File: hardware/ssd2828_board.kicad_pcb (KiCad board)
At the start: 4 copper layers, 91.3 x 53.5 mm, 144 parts, among them IC1 TLV62568DBVR, IC2 MIC5501-3.0YM5-TR, IC3 TPS65131TRGERQ1, J1 FH35C-25S-0.3SHW_50_, J2 FH35C-25S-0.3SHW_50_, J3 Conn_01x34, J4 245863050104829+, J5 503548-1220, J6 FH35C-25S-0.3SHW_50_, J7 FH35C-25S-0.3SHW_50_, J8 FH35C-25S-0.3SHW_50_, U1 SSD2828QN4, U2 PAM2306DYPAA, U3 MIC3289, U4 LP3320, Y1 24mhz

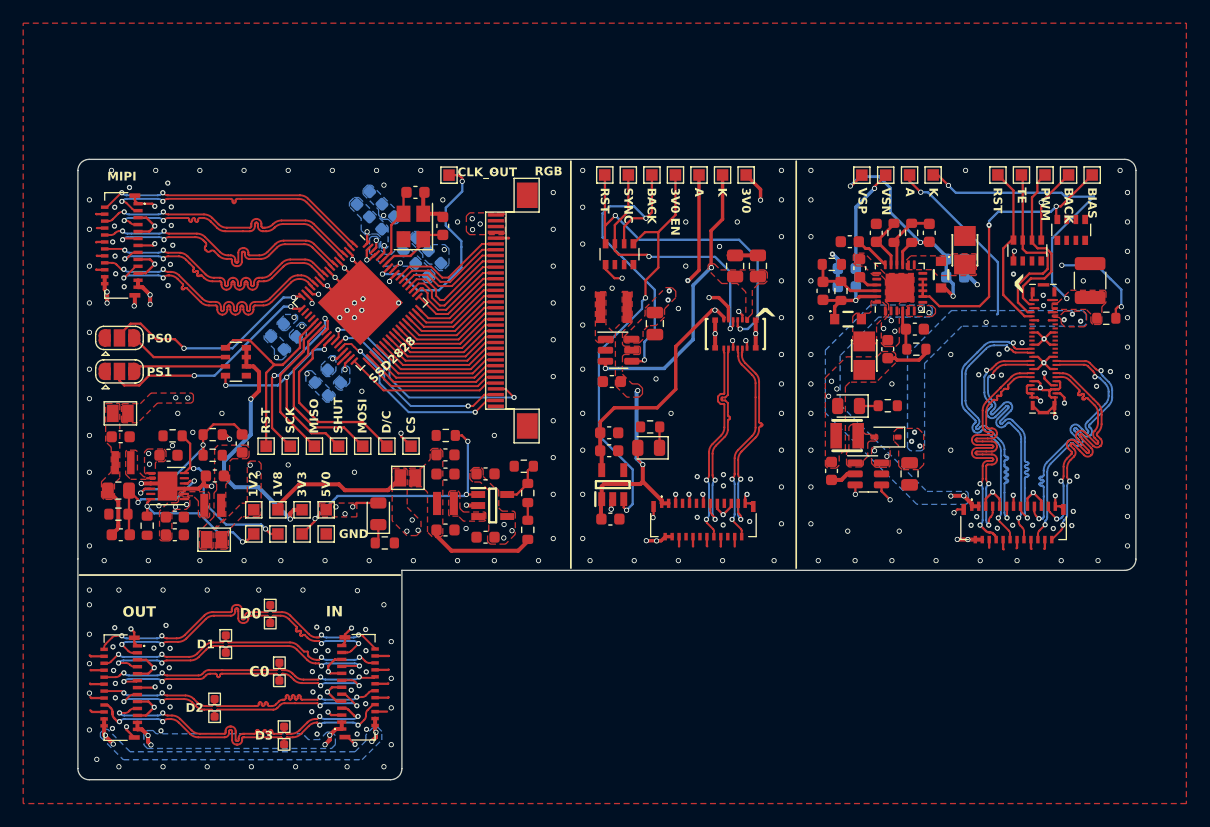
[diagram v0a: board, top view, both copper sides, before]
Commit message: added copper pour on back layer to adhere with jlcpcb guidelines
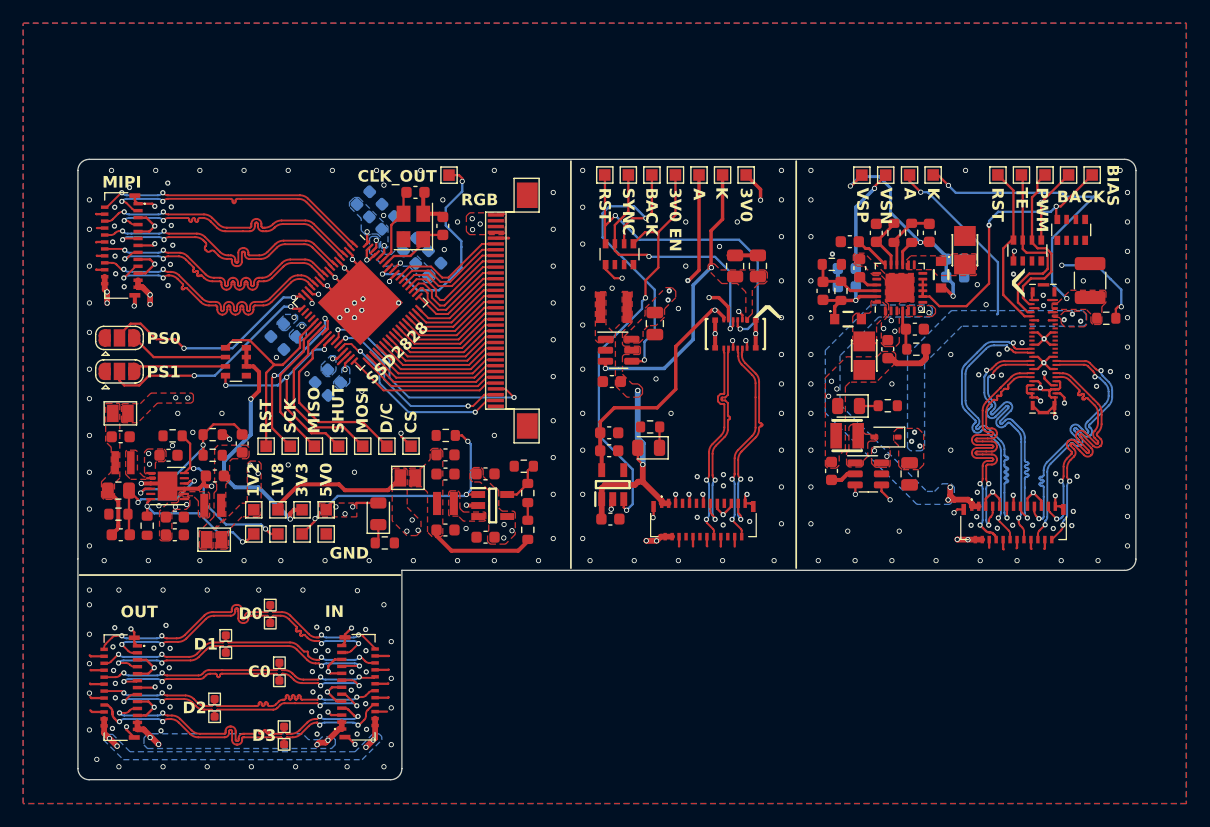
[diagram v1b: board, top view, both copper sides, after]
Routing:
- net GND: track 152.8 -> 148.4 mm
- net +5V: track 37.4 -> 39.9 mm
- net +1V8: track 81.4 -> 83.0 mm
- net /VS035ZSM/BIAS_EN: track 26.5 -> 25.8 mm

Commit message: fixed hirose FPC connector poinitng backwards on the 2 lcd boards+added stm32f401 boilerplate code
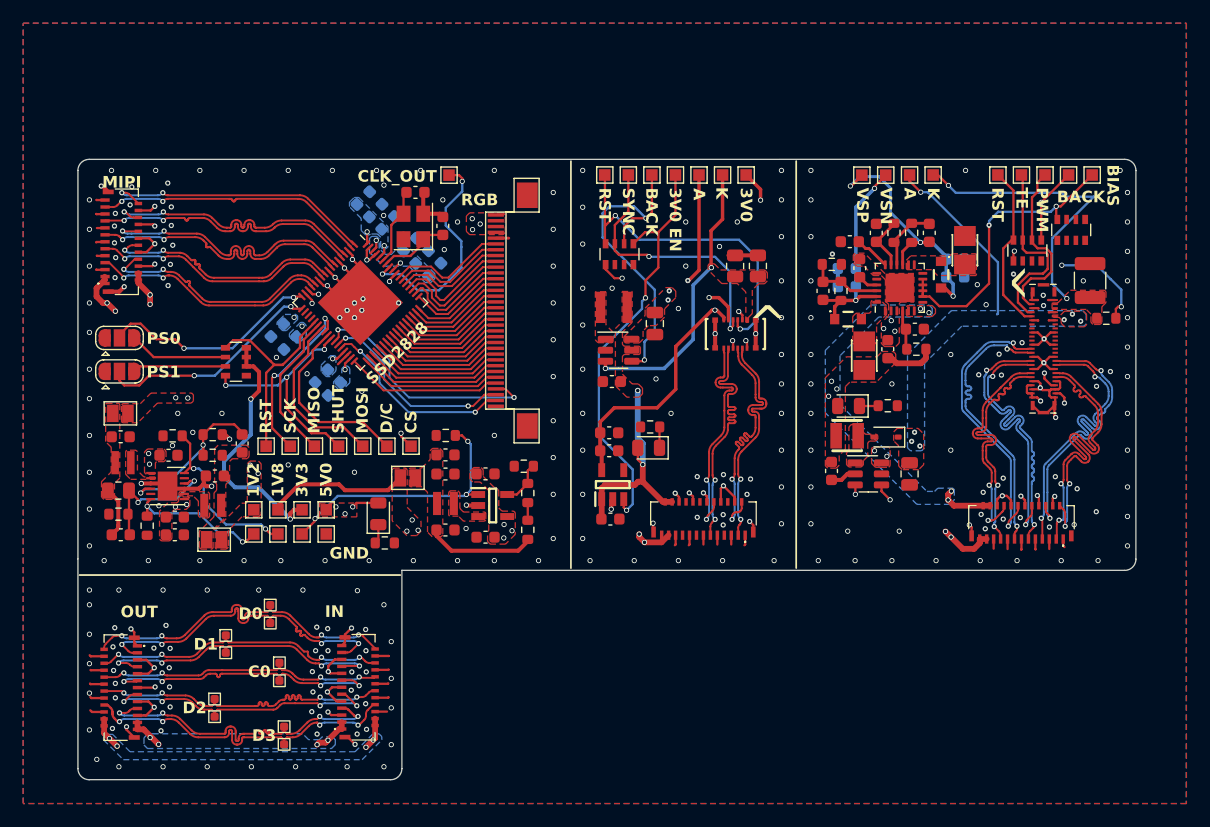
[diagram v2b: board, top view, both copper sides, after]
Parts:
- moved J2 0.69 mm to (133.1, 82.5), turned to 0 degrees
- moved J1 0.33 mm to (55.4, 58.2), turned to -90 degrees
- turned J8 to 0 degrees
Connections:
- J1 pad 1: GND -> +1V8
- J1 pad 10: /SSD2828/MIPI_CLK_P -> GND
- J1 pad 11: /SSD2828/MIPI_CLK_N -> /SSD2828/MIPI_DATA2_N
- J1 pad 12: GND -> /SSD2828/MIPI_DATA2_P
- J1 pad 14: /SSD2828/MIPI_DATA2_P -> GND
- J1 pad 15: /SSD2828/MIPI_DATA2_N -> /SSD2828/MIPI_CLK_N
- J1 pad 16: GND -> /SSD2828/MIPI_CLK_P
- J1 pad 18: /SSD2828/MIPI_DATA3_P -> GND
- J1 pad 19: /SSD2828/MIPI_DATA3_N -> /SSD2828/MIPI_DATA1_N
- J1 pad 2: /SSD2828/MIPI_DATA0_P -> +5V
- J1 pad 20: GND -> /SSD2828/MIPI_DATA1_P
- J1 pad 22: +1V8 -> GND
- J1 pad 23: +5V -> /SSD2828/MIPI_DATA0_N
- J1 pad 24: +1V8 -> /SSD2828/MIPI_DATA0_P
- J1 pad 25: +5V -> GND
- J1 pad 3: /SSD2828/MIPI_DATA0_N -> +1V8
- J1 pad 4: GND -> +5V
- J1 pad 6: /SSD2828/MIPI_DATA1_P -> GND
- J1 pad 7: /SSD2828/MIPI_DATA1_N -> /SSD2828/MIPI_DATA3_N
- J1 pad 8: GND -> /SSD2828/MIPI_DATA3_P
- J2 pad 1: +5V -> GND
- J2 pad 10: GND -> /VS035ZSM/MIPI_CLK_P
- J2 pad 11: /VS035ZSM/MIPI_DATA2_N -> /VS035ZSM/MIPI_CLK_N
- J2 pad 12: /VS035ZSM/MIPI_DATA2_P -> GND
- J2 pad 14: GND -> /VS035ZSM/MIPI_DATA2_P
- J2 pad 15: /VS035ZSM/MIPI_CLK_N -> /VS035ZSM/MIPI_DATA2_N
- J2 pad 16: /VS035ZSM/MIPI_CLK_P -> GND
- J2 pad 18: GND -> /VS035ZSM/MIPI_DATA3_P
- J2 pad 19: /VS035ZSM/MIPI_DATA1_N -> /VS035ZSM/MIPI_DATA3_N
- J2 pad 2: +1V8 -> /VS035ZSM/MIPI_DATA0_P
- J2 pad 20: /VS035ZSM/MIPI_DATA1_P -> GND
- J2 pad 22: GND -> +5V
- J2 pad 23: /VS035ZSM/MIPI_DATA0_N -> +1V8
- J2 pad 24: /VS035ZSM/MIPI_DATA0_P -> +5V
- J2 pad 25: GND -> +1V8
- J2 pad 3: +5V -> /VS035ZSM/MIPI_DATA0_N
- J2 pad 4: +1V8 -> GND
- J2 pad 6: GND -> /VS035ZSM/MIPI_DATA1_P
- J2 pad 7: /VS035ZSM/MIPI_DATA3_N -> /VS035ZSM/MIPI_DATA1_N
- J2 pad 8: /VS035ZSM/MIPI_DATA3_P -> GND
- J8 pad 1: +5V -> GND
- J8 pad 10: GND -> /LH154Q01/MIPI_CLK_P
- J8 pad 11: /LH154Q01/MIPI_DATA2_N -> /LH154Q01/MIPI_CLK_N
- J8 pad 12: /LH154Q01/MIPI_DATA2_P -> GND
- J8 pad 14: GND -> /LH154Q01/MIPI_DATA2_P
- J8 pad 15: /LH154Q01/MIPI_CLK_N -> /LH154Q01/MIPI_DATA2_N
- J8 pad 16: /LH154Q01/MIPI_CLK_P -> GND
- J8 pad 18: GND -> /LH154Q01/MIPI_DATA3_P
- J8 pad 19: /LH154Q01/MIPI_DATA1_N -> /LH154Q01/MIPI_DATA3_N
- J8 pad 2: +1V8 -> /LH154Q01/MIPI_DATA0_P
- J8 pad 20: /LH154Q01/MIPI_DATA1_P -> GND
- J8 pad 22: GND -> +5V
- J8 pad 23: /LH154Q01/MIPI_DATA0_N -> +1V8
- J8 pad 24: /LH154Q01/MIPI_DATA0_P -> +5V
- J8 pad 25: GND -> +1V8
- J8 pad 3: +5V -> /LH154Q01/MIPI_DATA0_N
- J8 pad 4: +1V8 -> GND
- J8 pad 6: GND -> /LH154Q01/MIPI_DATA1_P
- J8 pad 7: /LH154Q01/MIPI_DATA3_N -> /LH154Q01/MIPI_DATA1_N
- J8 pad 8: /LH154Q01/MIPI_DATA3_P -> GND
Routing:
- net /LH154Q01/MIPI_DATA0_P: track 18.0 -> 23.0 mm
- net /VS035ZSM/MIPI_DATA3_P: track 25.5 -> 20.7 mm
- net /VS035ZSM/MIPI_DATA3_N: track 25.4 -> 20.6 mm
- net /LH154Q01/MIPI_CLK_N: track 17.9 -> 22.5 mm
- net +1V8: track 83.0 -> 86.9 mm
- net /SSD2828/MIPI_DATA3_P: track 23.8 -> 20.7 mm
- net /SSD2828/MIPI_DATA3_N: track 23.8 -> 20.7 mm
- net /SSD2828/MIPI_DATA2_P: track 23.8 -> 21.1 mm
- net /SSD2828/MIPI_DATA2_N: track 23.8 -> 21.1 mm
- net /LH154Q01/MIPI_DATA0_N: track 18.0 -> 19.4 mm
- net /LH154Q01/MIPI_CLK_P: track 18.0 -> 19.4 mm
- net GND: track 148.4 -> 147.3 mm, vias 281 -> 282
- net +5V: track 39.9 -> 40.9 mm
- net /SSD2828/MIPI_DATA1_N: track 23.8 -> 24.3 mm

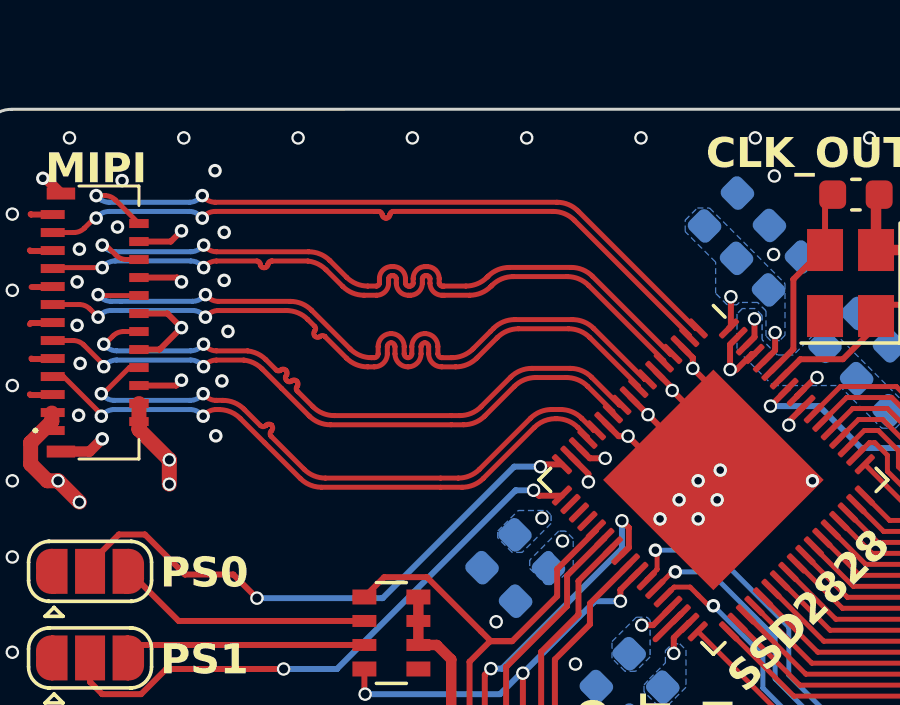
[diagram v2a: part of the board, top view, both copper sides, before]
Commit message: length tuned mipi lines on ssd2828 board
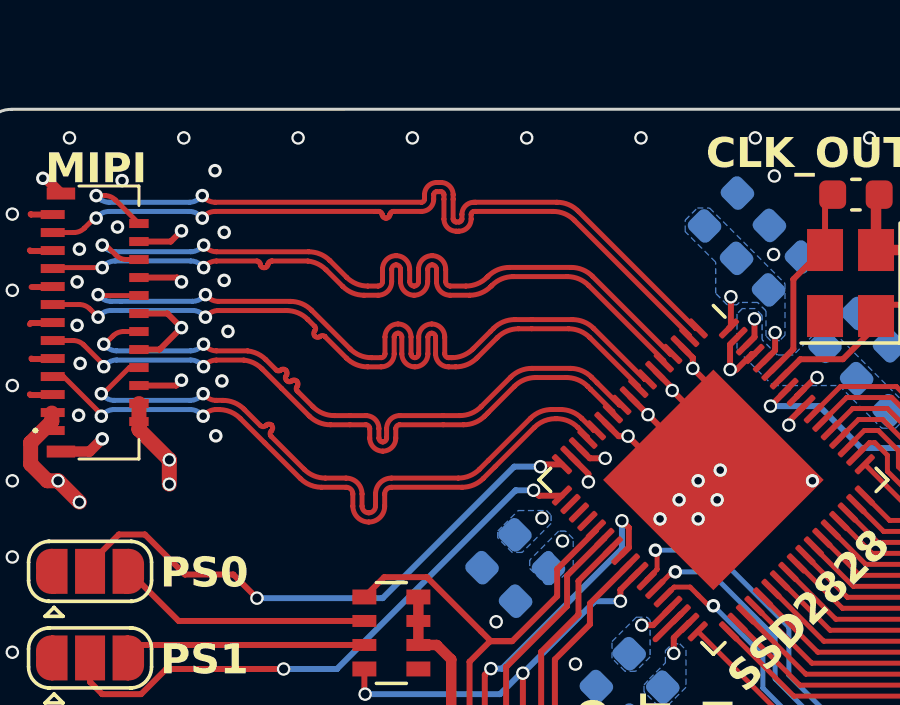
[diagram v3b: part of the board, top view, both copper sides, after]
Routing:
- net /SSD2828/MIPI_DATA0_N: track 23.8 -> 25.7 mm
- net /SSD2828/MIPI_DATA0_P: track 23.8 -> 25.7 mm
- net /SSD2828/MIPI_DATA3_N: track 20.7 -> 22.3 mm
- net /SSD2828/MIPI_DATA3_P: track 20.7 -> 22.3 mm
- net /SSD2828/MIPI_CLK_N: track 24.1 -> 25.4 mm
- net /SSD2828/MIPI_CLK_P: track 24.0 -> 25.3 mm
- net /SSD2828/MIPI_DATA1_N: track 24.3 -> 25.6 mm
- net /SSD2828/MIPI_DATA1_P: track 24.1 -> 25.4 mm
- net /SSD2828/MIPI_DATA2_P: track 21.1 -> 22.3 mm
- net /SSD2828/MIPI_DATA2_N: track 21.1 -> 22.3 mm

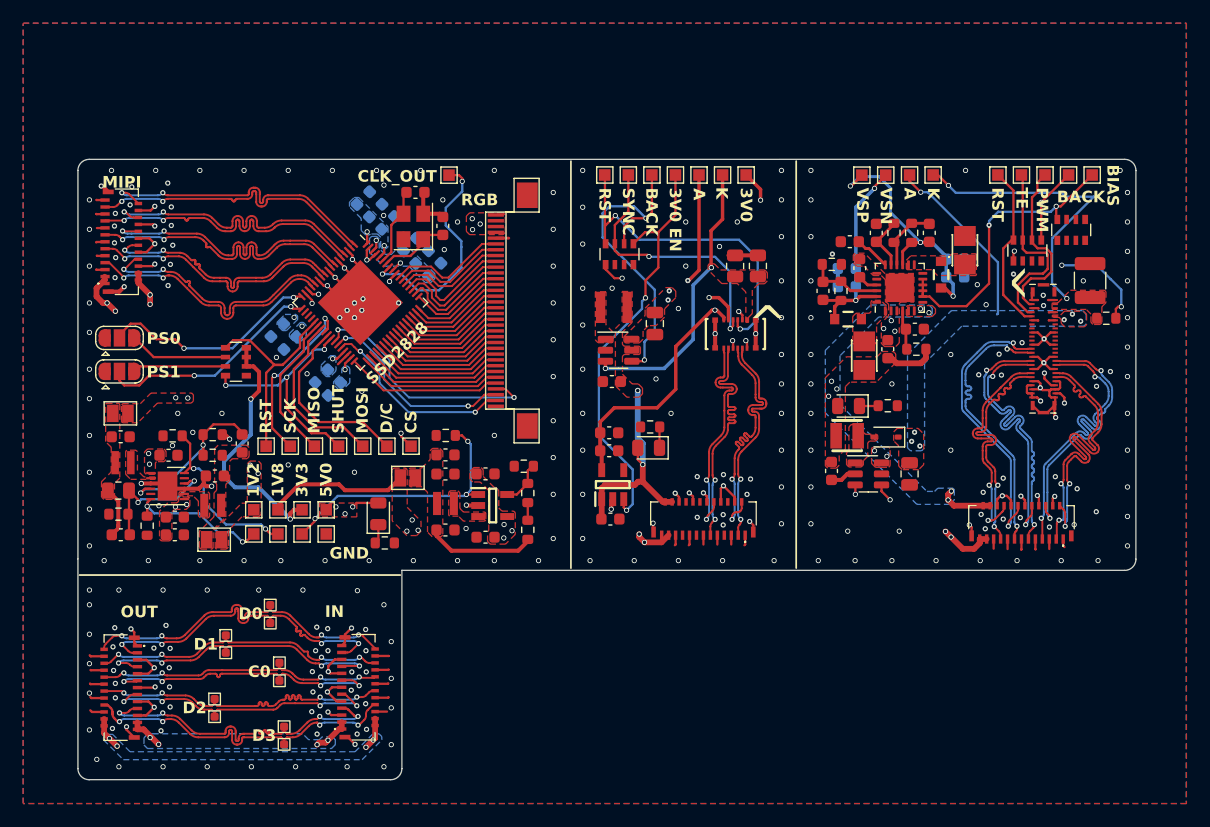
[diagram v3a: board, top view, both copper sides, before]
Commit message: updated readme + fixed pcb + cleaned up code
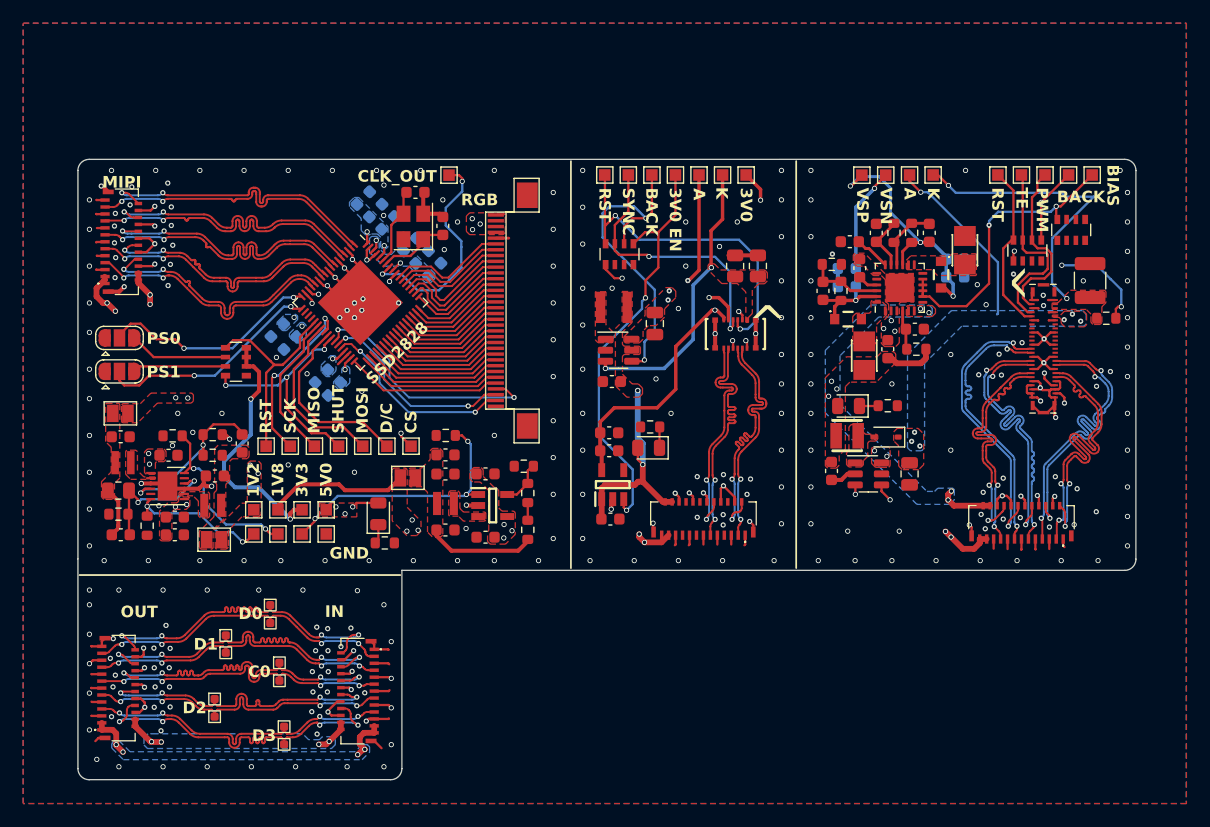
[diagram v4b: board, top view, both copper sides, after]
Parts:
- removed J6, J7: FH35C-25S-0.3SHW_50_, SamacSys_Parts:FH35C25S03SHW50
- added J10: FH35C-25S-0.3SHW_50_, SamacSys_Parts:FH35C25S03SHW50, F.Cu at (55.1, 96.7)
- added J9: FH35C-25S-0.3SHW_50_, SamacSys_Parts:FH35C25S03SHW50, F.Cu at (75.9, 97.0)
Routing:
- net /debug/MIPI_CLK_P: track 24.6 -> 29.8 mm
- net /debug/MIPI_DATA1_P: track 25.6 -> 29.8 mm
- net /debug/MIPI_DATA2_N: track 24.3 -> 26.6 mm
- net GND: track 147.3 -> 145.0 mm, vias 282 -> 280
- net +1V8: track 86.9 -> 89.1 mm
- net /debug/MIPI_DATA0_P: track 28.6 -> 30.7 mm
- net /debug/MIPI_DATA3_N: track 28.6 -> 26.6 mm
- net /debug/MIPI_CLK_N: track 24.6 -> 26.6 mm
- net /debug/MIPI_DATA0_N: track 28.6 -> 26.6 mm
- net /debug/MIPI_DATA3_P: track 29.0 -> 30.5 mm
- net /debug/MIPI_DATA1_N: track 25.6 -> 26.6 mm
- net /debug/MIPI_DATA2_P: track 27.3 -> 26.6 mm
